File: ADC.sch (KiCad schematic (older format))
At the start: 0 parts

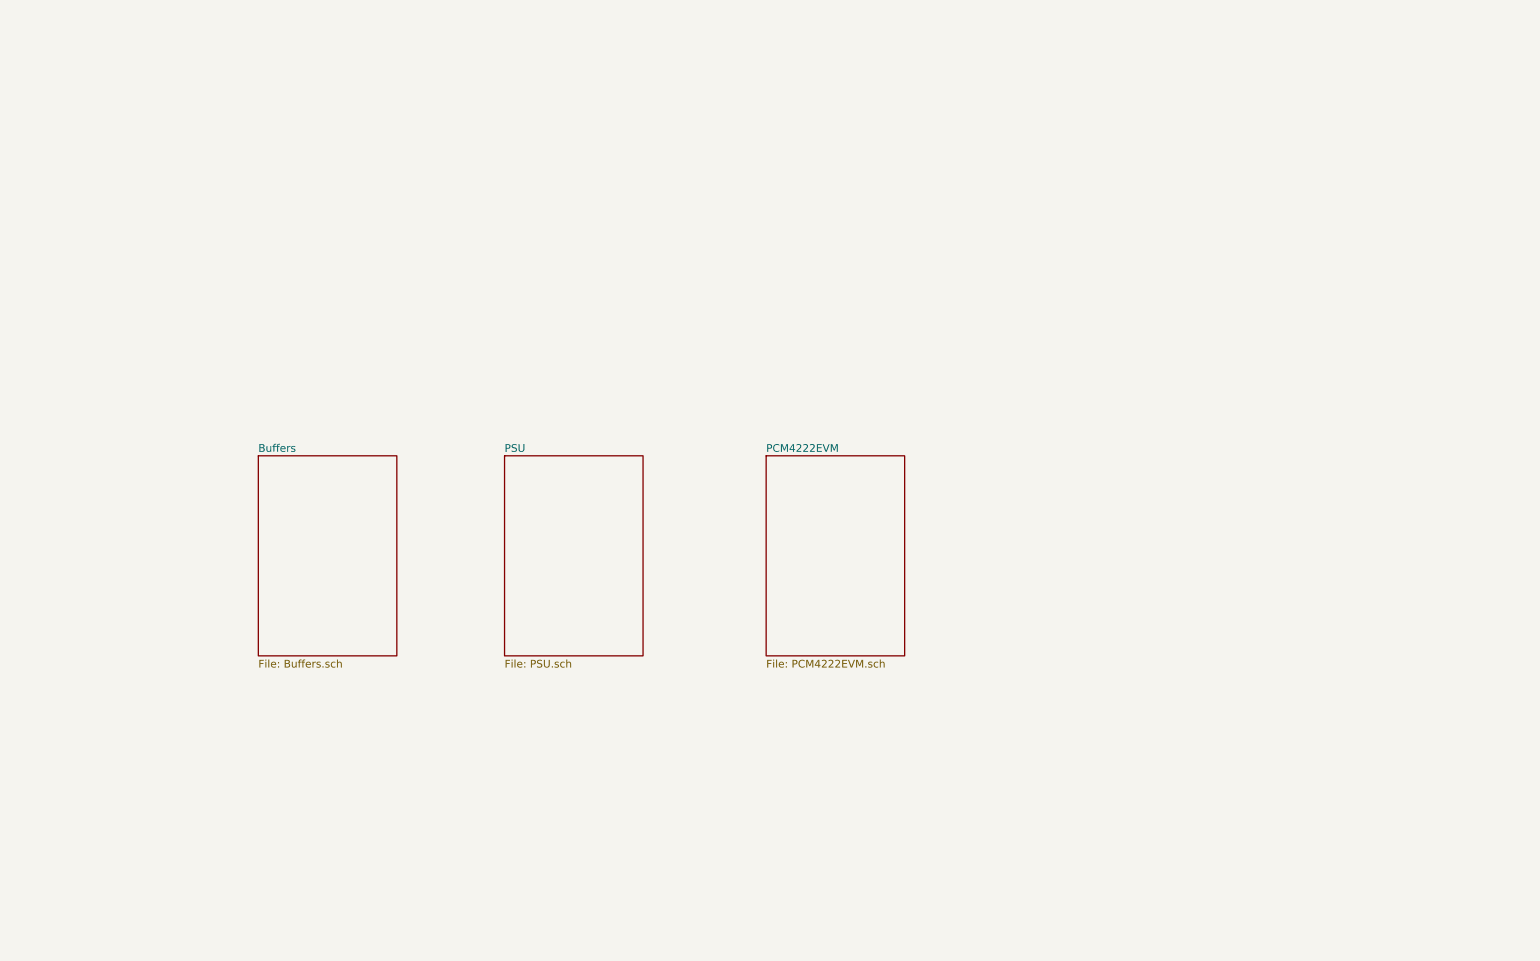
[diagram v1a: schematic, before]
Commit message: Started splitting the PSU into internal and external subsections.
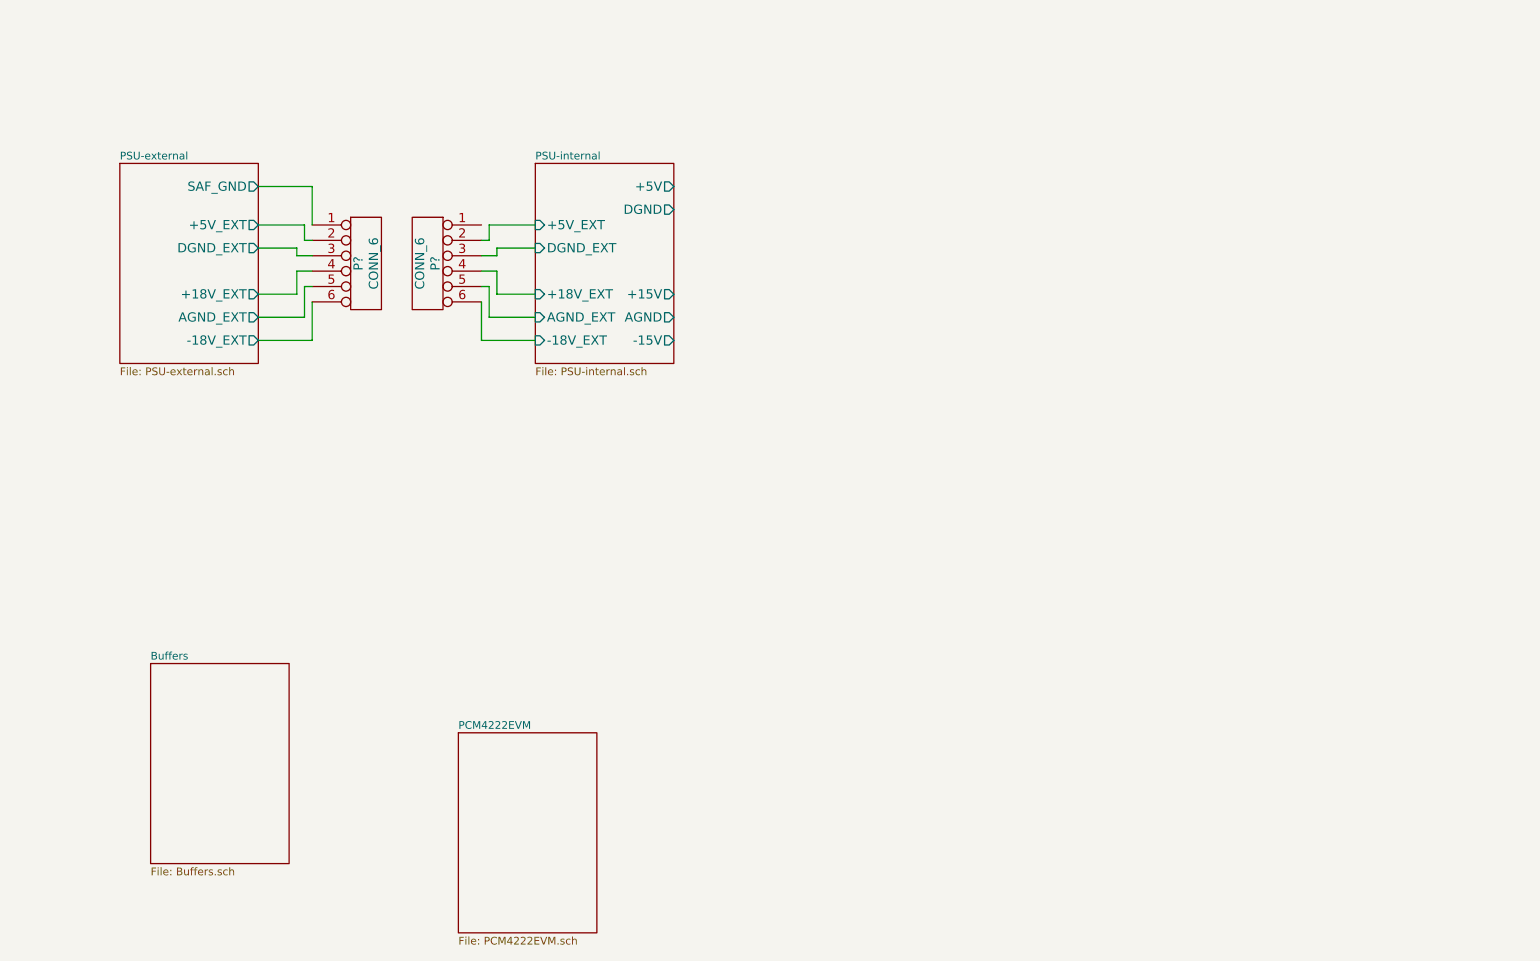
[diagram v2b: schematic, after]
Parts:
- added P? (x2): CONN_6, symbol CONN_6
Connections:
- new net PSU-external/+18V_EXT: P?.4
- new net PSU-external/+5V_EXT: P?.2
- new net PSU-external/-18V_EXT: P?.6
- new net PSU-external/AGND_EXT: P?.5
- new net PSU-external/DGND_EXT: P?.3
- new net PSU-external/SAF_GND: P?.1
- new net PSU-internal/+18V_EXT: P?.4
- new net PSU-internal/+5V_EXT: P?.2
- new net PSU-internal/-18V_EXT: P?.6
- new net PSU-internal/AGND_EXT: P?.5
- new net PSU-internal/DGND_EXT: P?.3
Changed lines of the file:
@@
 $Descr A4 11693 8268
 encoding utf-8
-Sheet 1 4
+Sheet 1 5
 Title ""
 Date "1 may 2014"
@@
 $EndDescr
 $Sheet
-S 5800 3300 900  1300
+S 3800 5100 900  1300
 U 535F19BB
 F0 "PCM4222EVM" 50
@@
 $EndSheet
 $Sheet
-S 4100 3300 900  1300
+S 4300 1400 900  1300
 U 535F19C2
-F0 "PSU" 50
-F1 "PSU.sch" 50
+F0 "PSU-internal" 50
+F1 "PSU-internal.sch" 50
+F2 "+5V_EXT" I L 4300 1800 60
+F3 "DGND_EXT" I L 4300 1950 60
+F4 "+18V_EXT" I L 4300 2250 60
+F5 "AGND_EXT" I L 4300 2400 60
+F6 "-18V_EXT" I L 4300 2550 60
+F7 "+15V" O R 5200 2250 60
+F8 "AGND" O R 5200 2400 60
+F9 "-15V" O R 5200 2550 60
+F10 "+5V" O R 5200 1550 60
+F11 "DGND" O R 5200 1700 60
 $EndSheet
 $Sheet
-S 2500 3300 900  1300
+S 1800 4650 900  1300
 U 535F19C9
 F0 "Buffers" 50
 F1 "Buffers.sch" 50
 $EndSheet
+$Sheet
+S 1600 1400 900  1300
+U 53688C29
+F0 "PSU-external" 50
+F1 "PSU-external.sch" 50
+F2 "+5V_EXT" O R 2500 1800 60
+F3 "+18V_EXT" O R 2500 2250 60
+F4 "AGND_EXT" O R 2500 2400 60
+F5 "-18V_EXT" O R 2500 2550 60
+F6 "DGND_EXT" O R 2500 1950 60
+F7 "SAF_GND" O R 2500 1550 60
+$EndSheet
+$Comp
+L CONN_6 P?
+U 1 1 5368BA3A
+P 3200 2050
+F 0 "P?" V 3150 2050 60  0000 C CNN
+F 1 "CONN_6" V 3250 2050 60  0000 C CNN
+F 2 "" H 3200 2050 60  0000 C CNN
+F 3 "" H 3200 2050 60  0000 C CNN
+	1    3200 2050
+	1    0    0    -1
+$EndComp
+$Comp
+L CONN_6 P?
+U 1 1 5368BCA4
+P 3600 2050
+F 0 "P?" V 3550 2050 60  0000 C CNN
+F 1 "CONN_6" V 3650 2050 60  0000 C CNN
+F 2 "" H 3600 2050 60  0000 C CNN
+F 3 "" H 3600 2050 60  0000 C CNN
+	1    3600 2050
+	-1   0    0    -1
+$EndComp
+Wire Wire Line
+	2500 1550 2850 1550
+Wire Wire Line
+	2850 1550 2850 1800
+Wire Wire Line
+	2500 1800 2800 1800
+Wire Wire Line
+	2800 1800 2800 1900
+Wire Wire Line
+	2800 1900 2850 1900
+Wire Wire Line
+	2500 1950 2750 1950
+Wire Wire Line
+	2750 1950 2750 2000
+Wire Wire Line
+	2750 2000 2850 2000
+Wire Wire Line
+	2500 2250 2750 2250
+Wire Wire Line
+	2750 2250 2750 2100
+Wire Wire Line
+	2750 2100 2850 2100
+Wire Wire Line
+	2500 2400 2800 2400
+Wire Wire Line
+	2800 2400 2800 2200
+Wire Wire Line
+	2800 2200 2850 2200
+Wire Wire Line
+	2500 2550 2850 2550
+Wire Wire Line
+	2850 2550 2850 2300
+Wire Wire Line
+	3950 2300 3950 2550
+Wire Wire Line
+	4000 2400 4000 2200
+Wire Wire Line
+	4000 2200 3950 2200
+Wire Wire Line
+	3950 2100 4050 2100
+Wire Wire Line
+	4050 2100 4050 2250
+Wire Wire Line
+	4050 1950 4050 2000
+Wire Wire Line
+	4050 2000 3950 2000
+Wire Wire Line
+	3950 1900 4000 1900
+Wire Wire Line
+	4000 1900 4000 1800
+Wire Wire Line
+	4000 1800 4300 1800
+Wire Wire Line
+	4300 1950 4050 1950
+Wire Wire Line
+	4050 2250 4300 2250
+Wire Wire Line
+	4300 2400 4000 2400
+Wire Wire Line
+	3950 2550 4300 2550
 $EndSCHEMATC

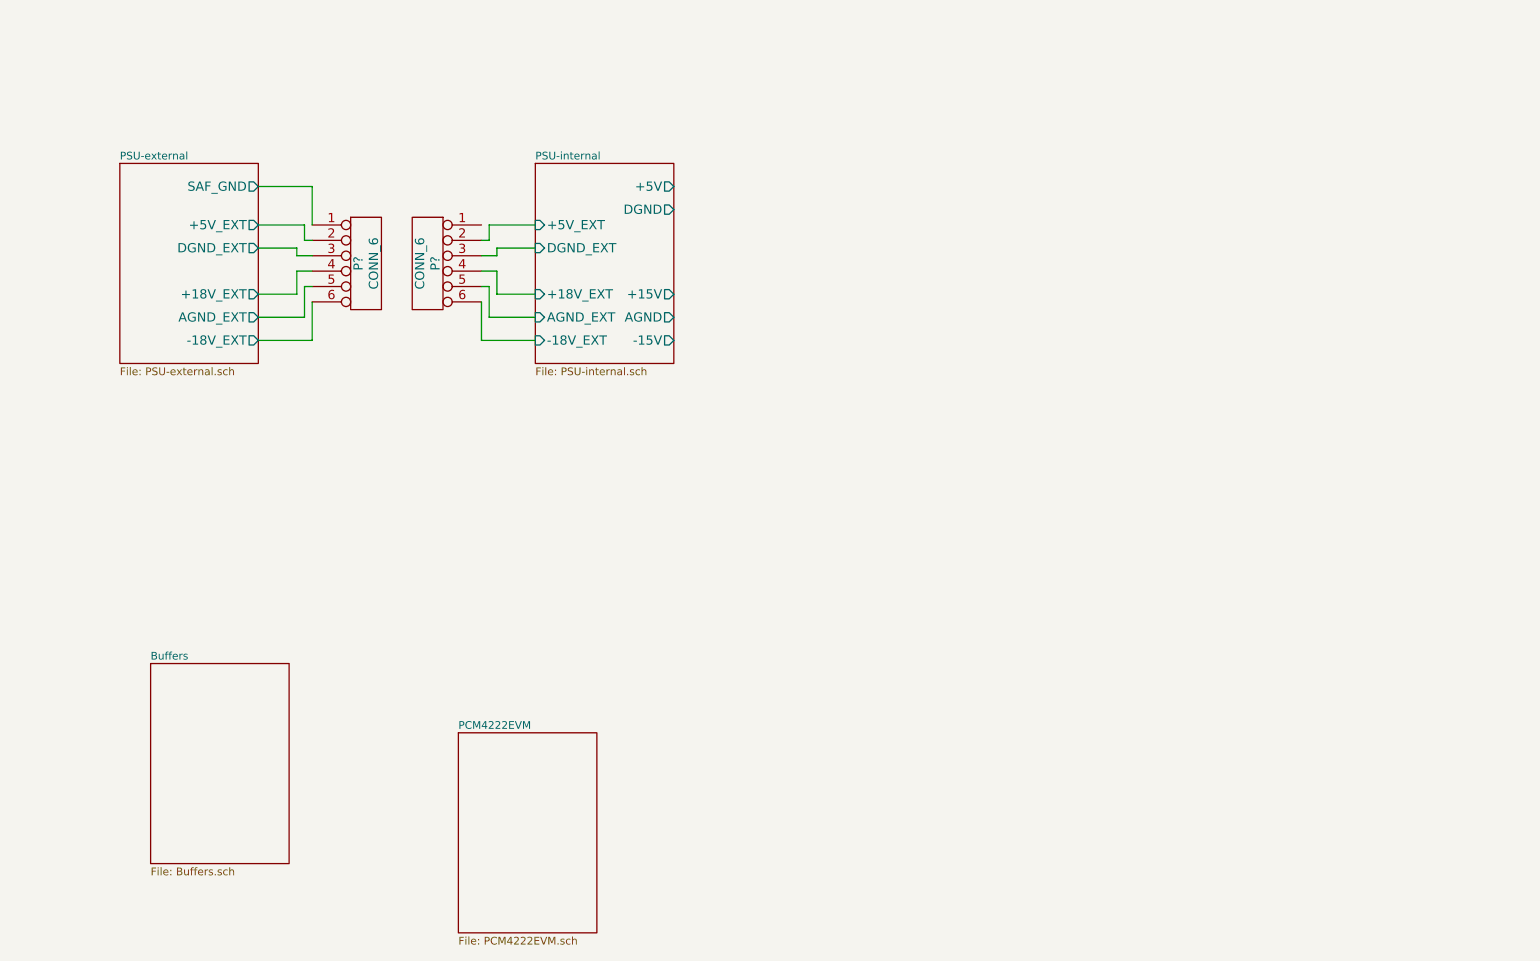
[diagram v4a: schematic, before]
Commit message: Completed the overall system layout, added clipping and input stages.
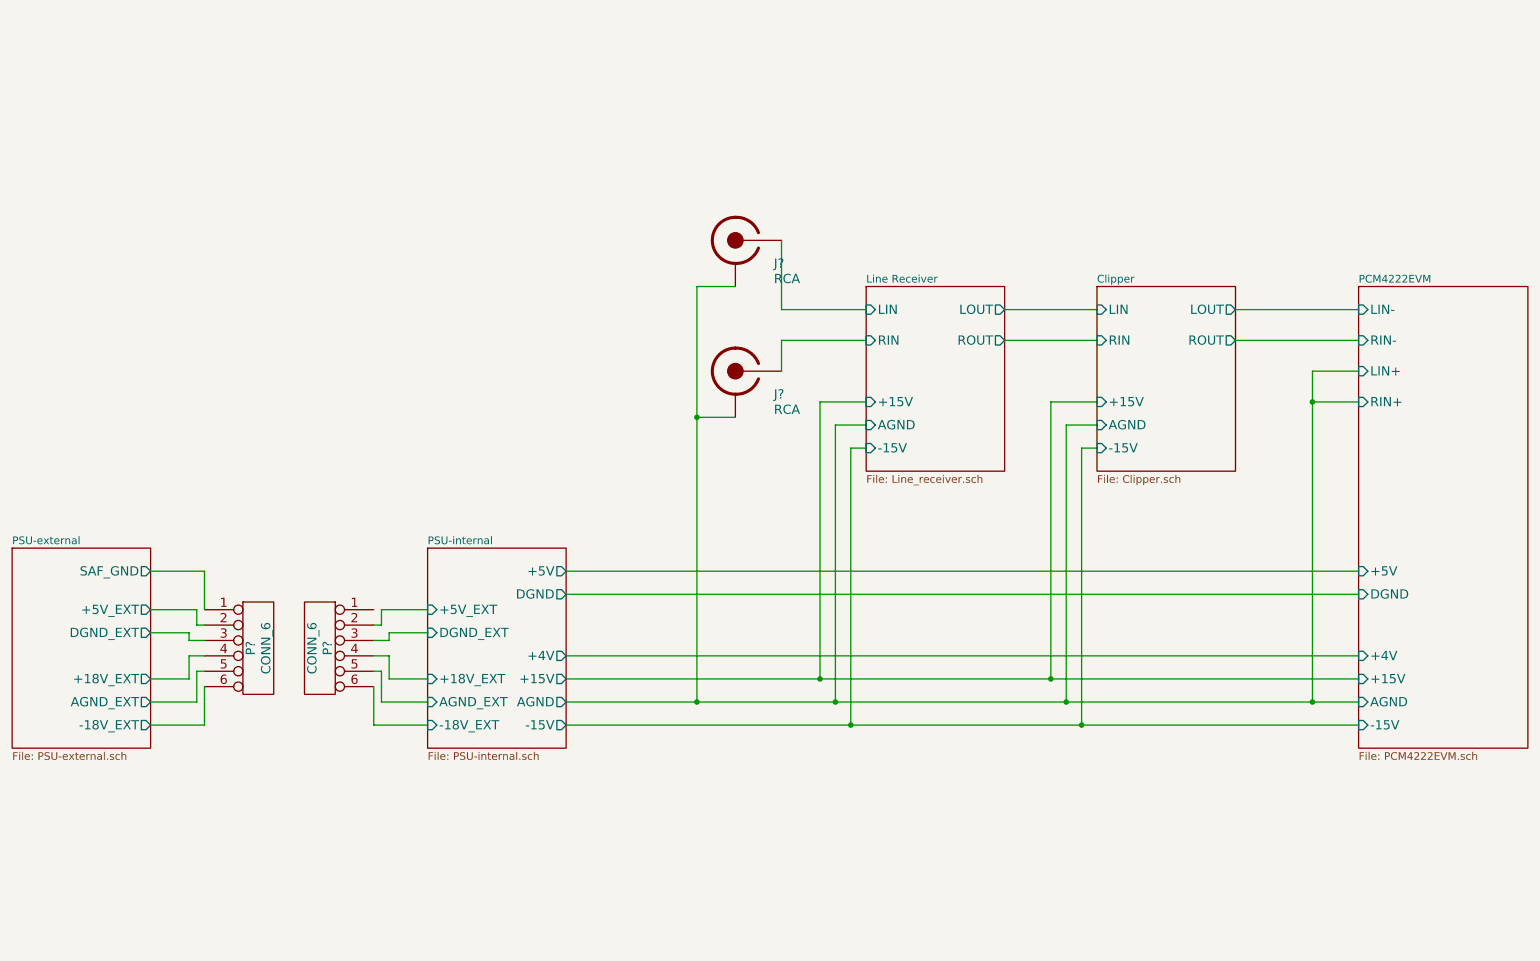
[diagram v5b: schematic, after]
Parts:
- added J? (x2): RCA, symbol RCA
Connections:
- new net Clipper/AGND: J?.~, J?.~
- new net Line Receiver/LIN: J?.~
- new net Line Receiver/RIN: J?.~
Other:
- moved on the sheet: P?
